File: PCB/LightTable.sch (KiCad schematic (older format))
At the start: 10 parts

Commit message: Working on a shield
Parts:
- removed C? (x2): 22pF, symbol C
- removed IC?: ATTINY85-P, DIP8, symbol ATTINY85-P
- removed R?: R, symbol R
- removed RV?: POT, symbol POT
- removed U?: ICSP, symbol ICSP
- removed X?: CRYSTAL, symbol CRYSTAL
- added CON1: BARREL_JACK, symbol BARREL_JACK
- added EN1: ENCODER_5_PINS, symbol ENCODER_5_PINS
- added K1: CONN_3_V, borniers:bornier3_V, symbol CONN_3_V
- added R1: 10K, Resistors_ThroughHole:Resistor_Horizontal_RM10mm, symbol R
- added SHIELD1: ARDUINO_SHIELD, arduino_shields:ARDUINO_SHIELD_2_040pins, symbol ARDUINO_SHIELD
- added U1, U2, U3: MosfetIRF, symbol MosfetIRF
- C1, C2: renamed from C?; footprint (none) -> Capacitors_ThroughHole:C_Disc_D3_P2.5; symbol C -> C-RESCUE-LightTable
- gave numbers to parts that had none: 1
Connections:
- net labels added: B, G, PBtn, PWM_R, R, V5
- wire segments 23 -> 41
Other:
- moved on the sheet: U4

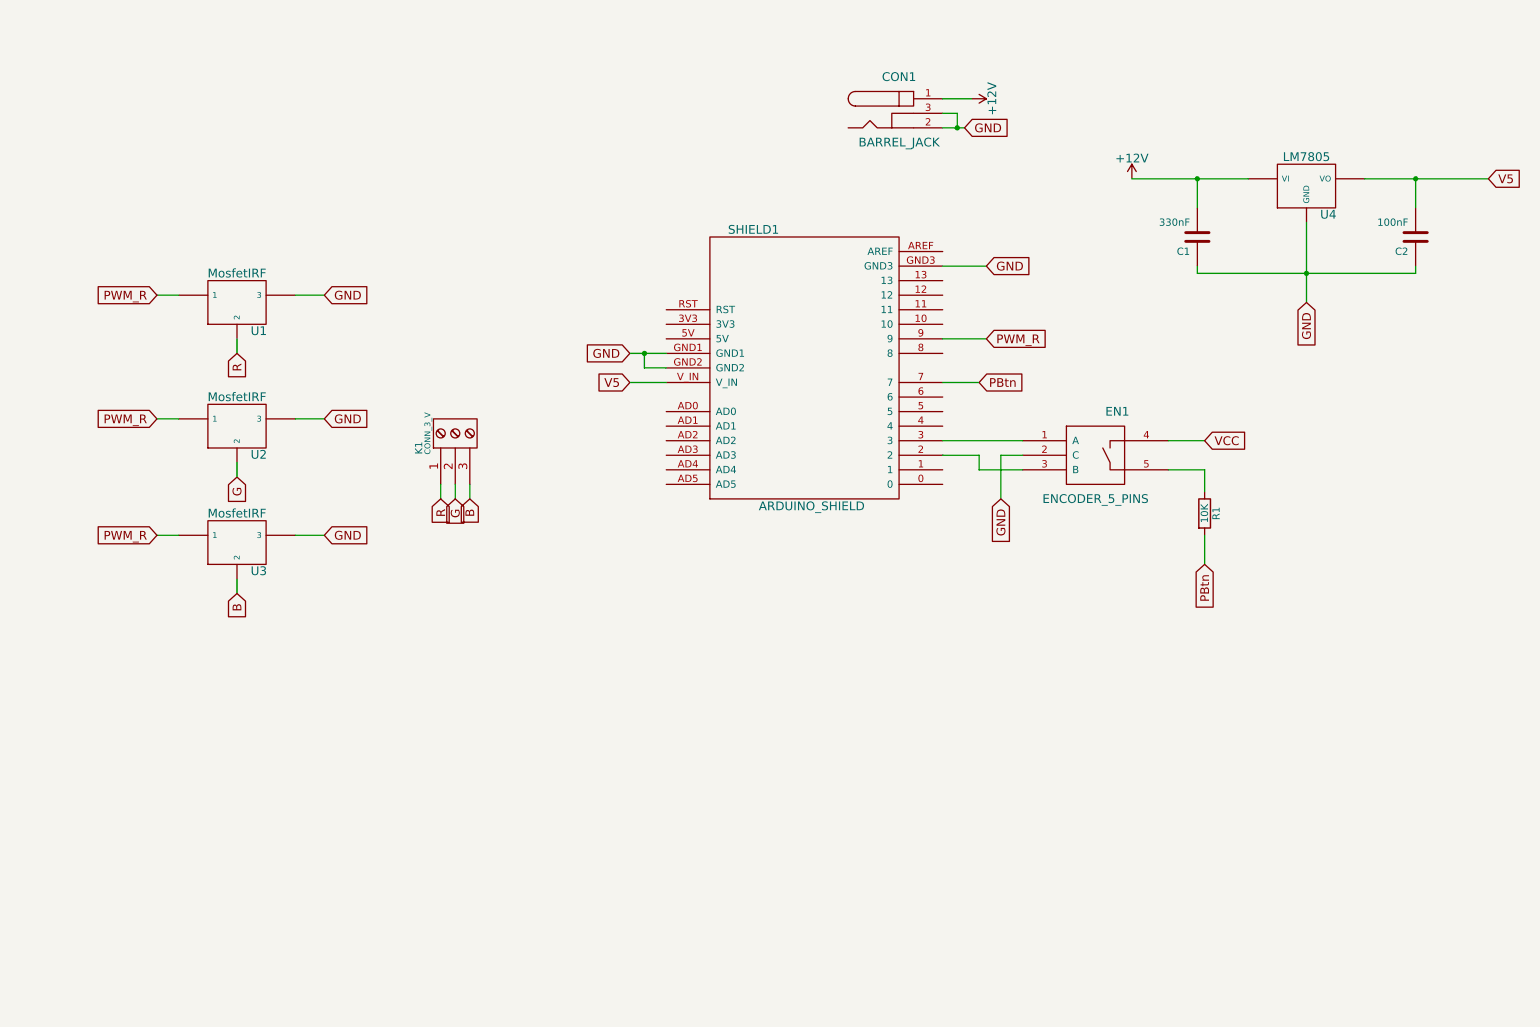
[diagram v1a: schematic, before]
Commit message: Added pcb layout and libraries
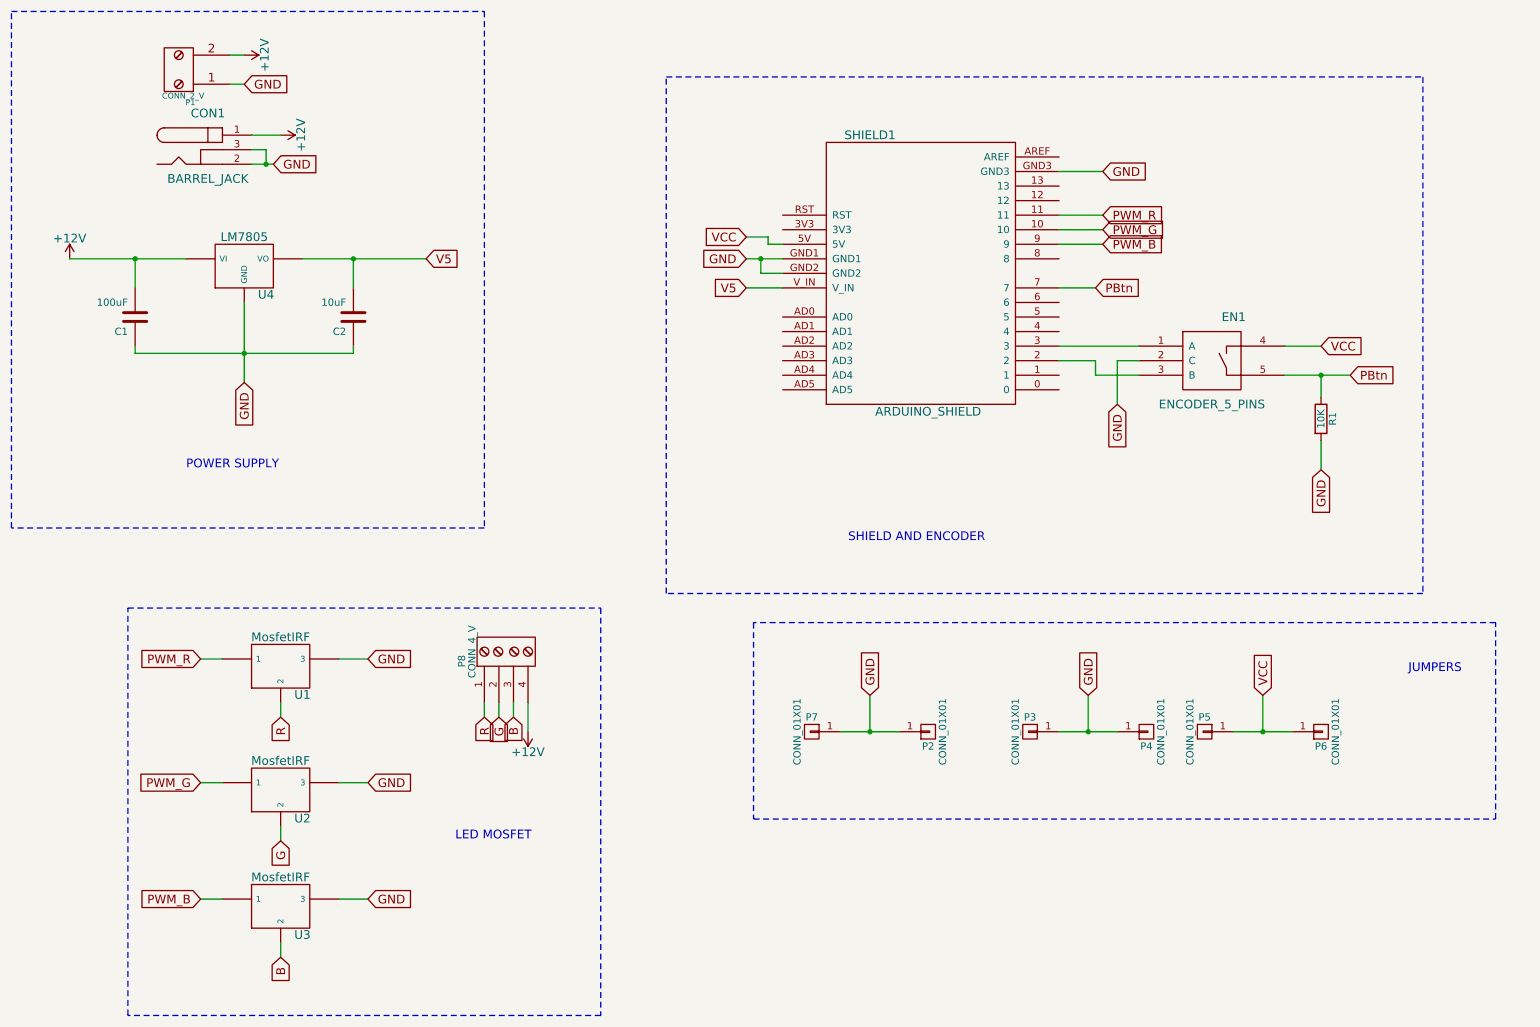
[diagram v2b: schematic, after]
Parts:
- removed K1: CONN_3_V, borniers:bornier3_V, symbol CONN_3_V
- added P1: CONN_2_V, borniers:bornier2_V, symbol CONN_2_V
- added P2, P3, P4, P5, P6, P7: CONN_01X01, library:header1x01, symbol CONN_01X01
- added P8: CONN_4_V, borniers:bornier4_V, symbol CONN_4_V
- C1: value 330nF -> 100uF
- C2: value 100nF -> 10uF
- CON1: footprint (none) -> library:BARREL_JACK
- EN1: footprint (none) -> library:ENCODER_5_PINS
- U1, U2, U3: footprint (none) -> library:IRF3205
- U4: footprint (none) -> library:LM7805
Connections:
- net +12V: now also P1.2 (P2), P8.4 (P4)
- net B: now also P8.3 (P3)
- net G: now also P8.2 (P2)
- net GND: now also R1.2, P1.1 (P1), P2.1 (P1), P3.1 (P1), P4.1 (P1), P7.1 (P1)
- net PBtn: now also EN1.5, R1.1; no longer R1.2
- net PWM_R: now also SHIELD1.11; no longer SHIELD1.9, U2.1, U3.1
- net R: now also P8.1 (P1)
- net VCC: now also SHIELD1.5V, P5.1 (P1), P6.1 (P1)
- net PWM_G: now reaches SHIELD1.10
- net PWM_G: now also U2.1
- new net PWM_B: SHIELD1.9, U3.1
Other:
- note added: "JUMPERS"
- note added: "LED MOSFET"
- note added: "POWER SUPPLY\n"
- note added: "SHIELD AND ENCODER"
- moved on the sheet: C1, C2, CON1, EN1, R1, SHIELD1, U1, U2, U3, U4

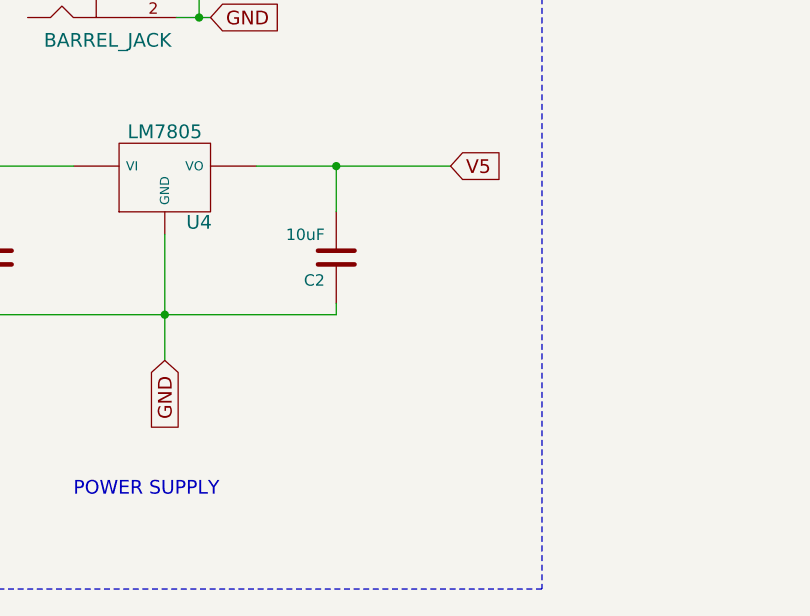
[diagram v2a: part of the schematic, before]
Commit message: Added Power Led and BOM
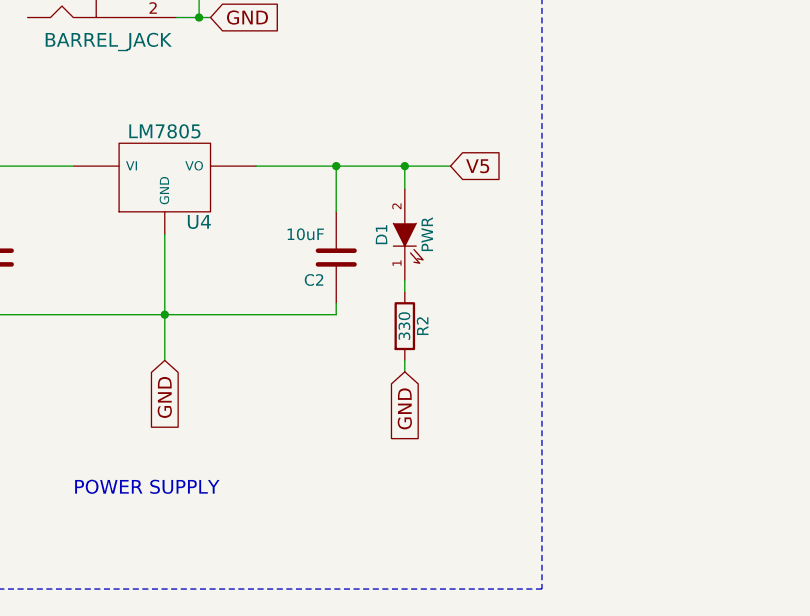
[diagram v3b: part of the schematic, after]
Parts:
- added D1: PWR, LEDs:LED-5MM, symbol LED
- added R2: 330, Resistors_ThroughHole:Resistor_Horizontal_RM10mm, symbol R
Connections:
- net GND: now also R2.2
- net V5: now also D1.2 (A)
- new net: D1.1 (K), R2.1
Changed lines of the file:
@@
 Wire Wire Line
 	4100 5550 4100 5350
+$Comp
+L LED D1
+U 1 1 55CC841D
+P 3200 2600
+F 0 "D1" H 3200 2700 50  0000 C CNN
+F 1 "PWR" H 3200 2500 50  0000 C CNN
+F 2 "LEDs:LED-5MM" H 3200 2600 60  0001 C CNN
+F 3 "" H 3200 2600 60  0000 C CNN
+	1    3200 2600
+	0    -1   -1   0
+$EndComp
+Connection ~ 3200 2300
+$Comp
+L R R2
+U 1 1 55CC852C
+P 3200 3000
+F 0 "R2" V 3280 3000 50  0000 C CNN
+F 1 "330" V 3200 3000 50  0000 C CNN
+F 2 "Resistors_ThroughHole:Resistor_Horizontal_RM10mm" V 3130 3000 30  0001 C CNN
+F 3 "" H 3200 3000 30  0000 C CNN
+	1    3200 3000
+	1    0    0    -1
+$EndComp
+Text GLabel 3200 3200 3    60   Input ~ 0
+GND
+Wire Wire Line
+	3200 3200 3200 3150
+Wire Wire Line
+	3200 2850 3200 2800
+Wire Wire Line
+	3200 2400 3200 2300
 $EndSCHEMATC

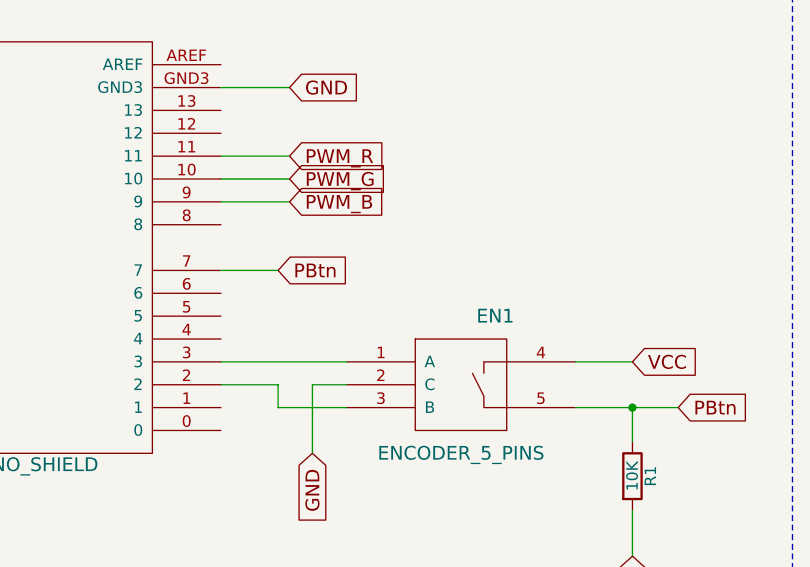
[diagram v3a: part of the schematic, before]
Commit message: Added led for showing when a long click has been made
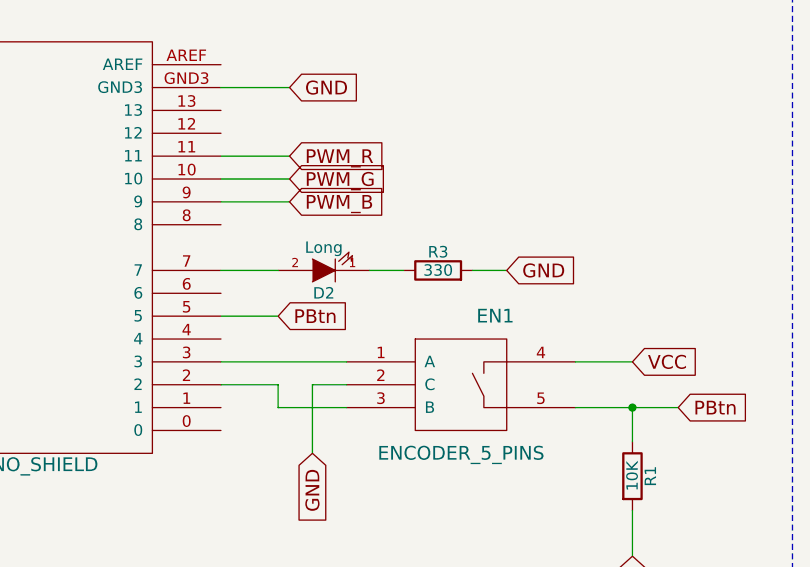
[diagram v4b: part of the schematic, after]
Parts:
- added D2: Long, LEDs:LED-5MM, symbol LED
- added R3: 330, Resistors_ThroughHole:Resistor_Horizontal_RM10mm, symbol R
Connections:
- net GND: now also R3.2
- net PBtn: now also SHIELD1.5; no longer SHIELD1.7
- new net: D2.2 (A), SHIELD1.7
- new net: D2.1 (K), R3.1
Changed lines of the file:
@@
 Wire Wire Line
 	9550 3750 9550 3550
-Text GLabel 8000 2500 2    60   Input ~ 0
-PBtn
 Wire Wire Line
 	8000 2500 7750 2500
@@
 Wire Wire Line
 	3200 2400 3200 2300
+Text GLabel 8000 2700 2    60   Input ~ 0
+PBtn
+Wire Wire Line
+	8000 2700 7750 2700
+$Comp
+L LED D2
+U 1 1 55D1C885
+P 8200 2500
+F 0 "D2" H 8200 2600 50  0000 C CNN
+F 1 "Long" H 8200 2400 50  0000 C CNN
+F 2 "LEDs:LED-5MM" H 8200 2500 60  0001 C CNN
+F 3 "" H 8200 2500 60  0000 C CNN
+	1    8200 2500
+	-1   0    0    1
+$EndComp
+$Comp
+L R R3
+U 1 1 55D1C88B
+P 8700 2500
+F 0 "R3" V 8780 2500 50  0000 C CNN
+F 1 "330" V 8700 2500 50  0000 C CNN
+F 2 "Resistors_ThroughHole:Resistor_Horizontal_RM10mm" V 8630 2500 30  0001 C CNN
+F 3 "" H 8700 2500 30  0000 C CNN
+	1    8700 2500
+	0    -1   -1   0
+$EndComp
+Text GLabel 9000 2500 2    60   Input ~ 0
+GND
+Wire Wire Line
+	8550 2500 8400 2500
+Wire Wire Line
+	8850 2500 9000 2500
 $EndSCHEMATC
